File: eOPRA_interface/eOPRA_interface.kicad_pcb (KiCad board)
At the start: 4 copper layers, 75 x 50 mm, 256 parts, among them J1 CONN_01X04_MALE, J2 CONN_01X04_MALE, J3 CONN_01X04_MALE, J4 CONN_01X02_MALE, J5 CONN_01X04_MALE, J6 CONN_02X10, J7 CONN_01X04_MALE, J8 CONN_01X04_MALE, Q1 G3VM-351VY1-TR05, Q10 RU1J002YNTCL, Q11 G3VM-351VY1-TR05, Q12 RU1J002YNTCL, Q13 RU1J002YNTCL, Q14 G3VM-351VY1-TR05, Q15 G3VM-351VY1-TR05, Q16 RU1J002YNTCL, Q17 G3VM-351VY1-TR05, Q18 G3VM-351VY1-TR05, Q19 RU1J002YNTCL, Q2 RU1J002YNTCL, Q20 G3VM-351VY1-TR05, Q21 RU1J002YNTCL, Q22 G3VM-351VY1-TR05, Q23 G3VM-351VY1-TR05, Q24 RU1J002YNTCL, Q25 RU1J002YNTCL, Q26 G3VM-351VY1-TR05, Q27 G3VM-351VY1-TR05, Q28 RU1J002YNTCL, Q29 RU1J002YNTCL, Q3 RU1J002YNTCL, Q30 G3VM-351VY1-TR05, Q31 G3VM-351VY1-TR05, Q32 RU1J002YNTCL, Q33 RU1J002YNTCL, Q34 G3VM-351VY1-TR05, Q4 RU1J002YNTCL, Q5 Q_PMOS_GSD, Q6 RU1J002YNTCL, Q7 G3VM-351VY1-TR05, Q8 RU1J002YNTCL, Q9 G3VM-351VY1-TR05, SW1 SW_Push, SW2 SW_Push, SW3 SW_Push, SW5 SW_Push, SW6 SW_Push, SW7 Rotary_Encoder_Switch, U1 USB_C_2.0, U10 RP2040, U11 W25Q128JVP, U13 MCP25625, U14 AP2205-50, U15 AP2213-8_SOIC, U2 ARM-SWD-10, U3 AP2213-8_SOIC, U4 DS3231MZ+, U5 XT-X, U6 Mounting-holes, U7 Mounting-holes, U8 Mounting-holes, U9 Mounting-holes, Y1 16Mhz 12pF, Y3 12Mhz 12pF

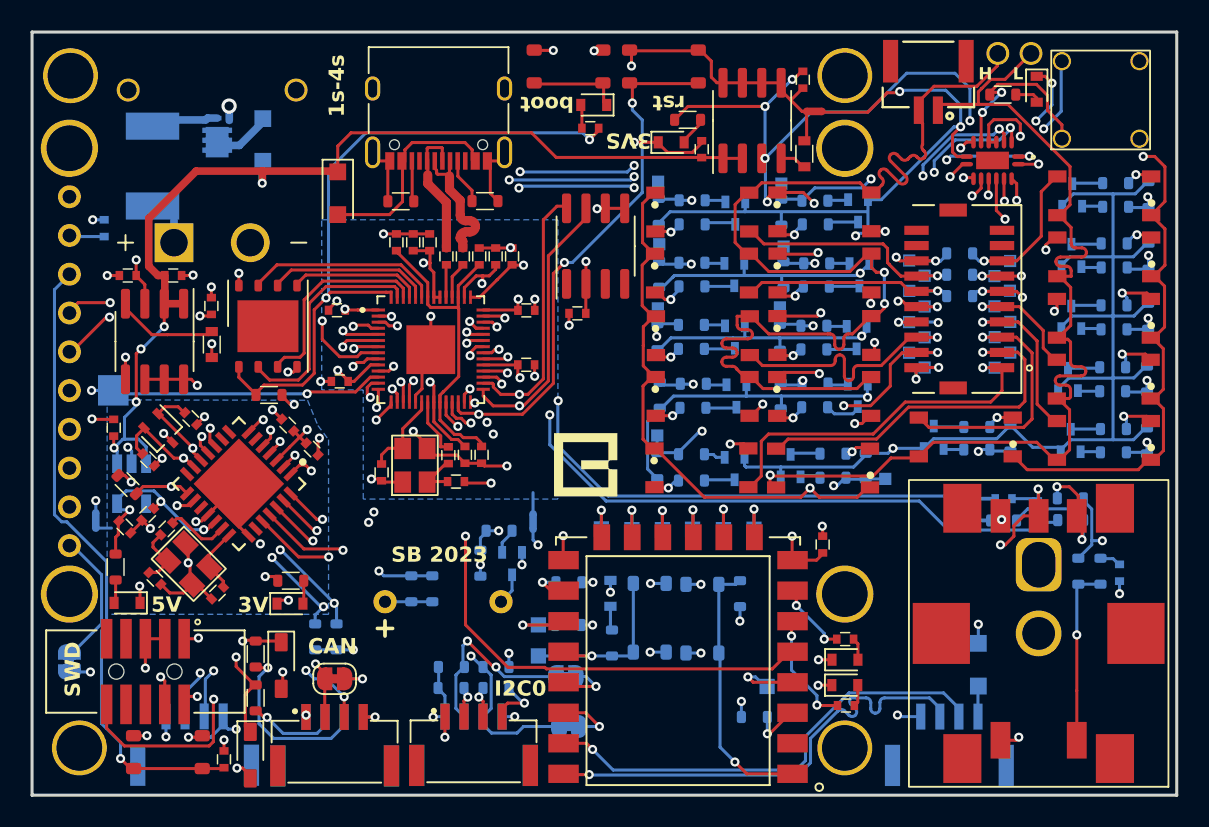
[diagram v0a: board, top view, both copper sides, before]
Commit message: fixed mounting holes
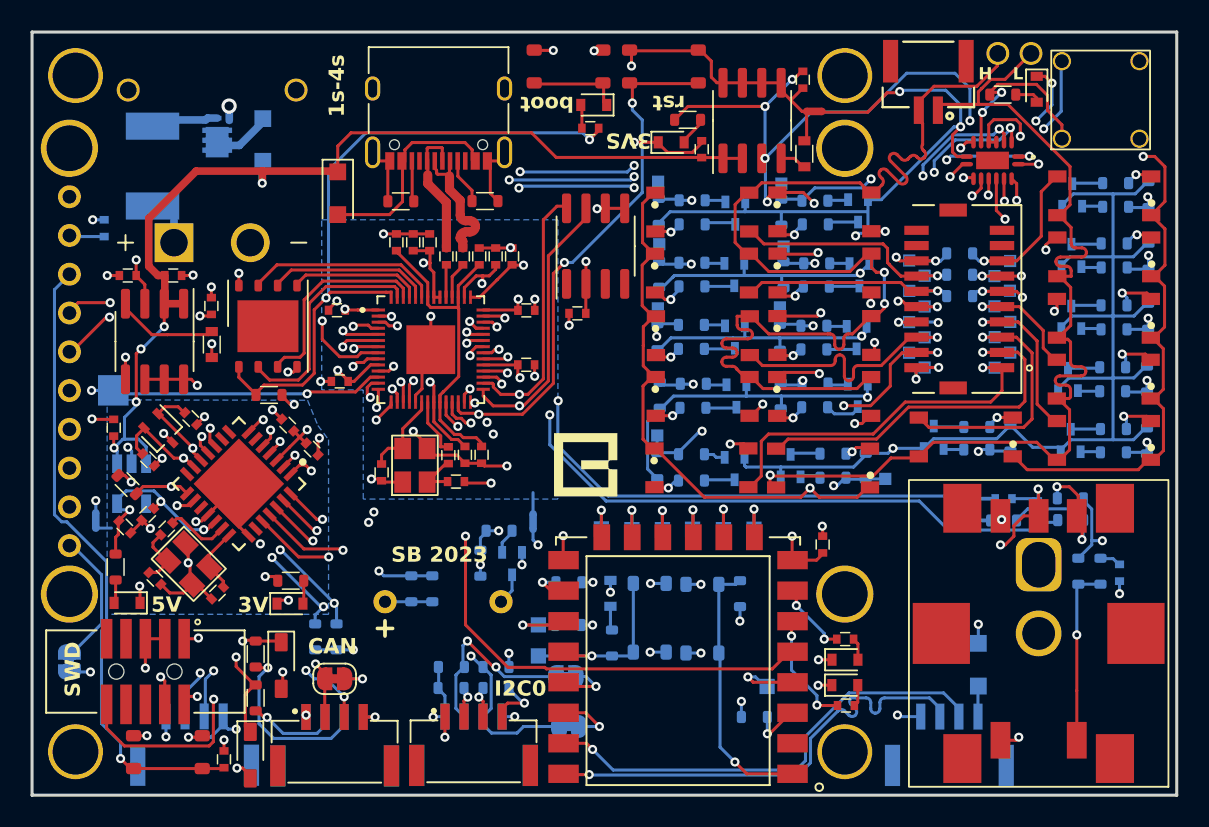
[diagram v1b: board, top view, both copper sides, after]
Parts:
- moved U6 0.35 mm to (102.8, 122.2)
- moved U9 0.33 mm to (102.8, 77.8)
- moved U8 0.25 mm to (153.2, 122.2)
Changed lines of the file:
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@@
   )
   (footprint "0_misc:plated_hole_3.0x3.6mm" (layer "F.Cu")
-    (at 153.25 121.9)
+    (at 153.25 122.15)
     (property "Sheetfile" "eOPRA_interface.kicad_sch")
     (property "Sheetname" "")
@@
   )
   (footprint "0_misc:plated_hole_3.0x3.6mm" (layer "F.Cu")
-    (at 103.1 121.9)
+    (at 102.85 122.15)
     (property "Sheetfile" "eOPRA_interface.kicad_sch")
     (property "Sheetname" "")
@@
   )
   (footprint "0_misc:plated_hole_3.0x3.6mm" (layer "F.Cu")
-    (at 102.52 77.858175)
+    (at 102.85 77.85)
     (property "Sheetfile" "eOPRA_interface.kicad_sch")
     (property "Sheetname" "")
